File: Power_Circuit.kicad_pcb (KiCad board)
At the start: 2 copper layers, 168.9 x 77.5 mm, 45 parts, among them J1 Conn_01x09, J2 Conn_01x04, K1 DSP1A-L2-DC5V, Q1 IRF7606PBF_3PINS_BWOUF, SW1 SW_Push, SW2 SW_STARTER, U1 B_Plug_Battery_In, U10 DSN2596, U11 B_Plug_12v_Motor1, U12 B_Plug_12v_Motor2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

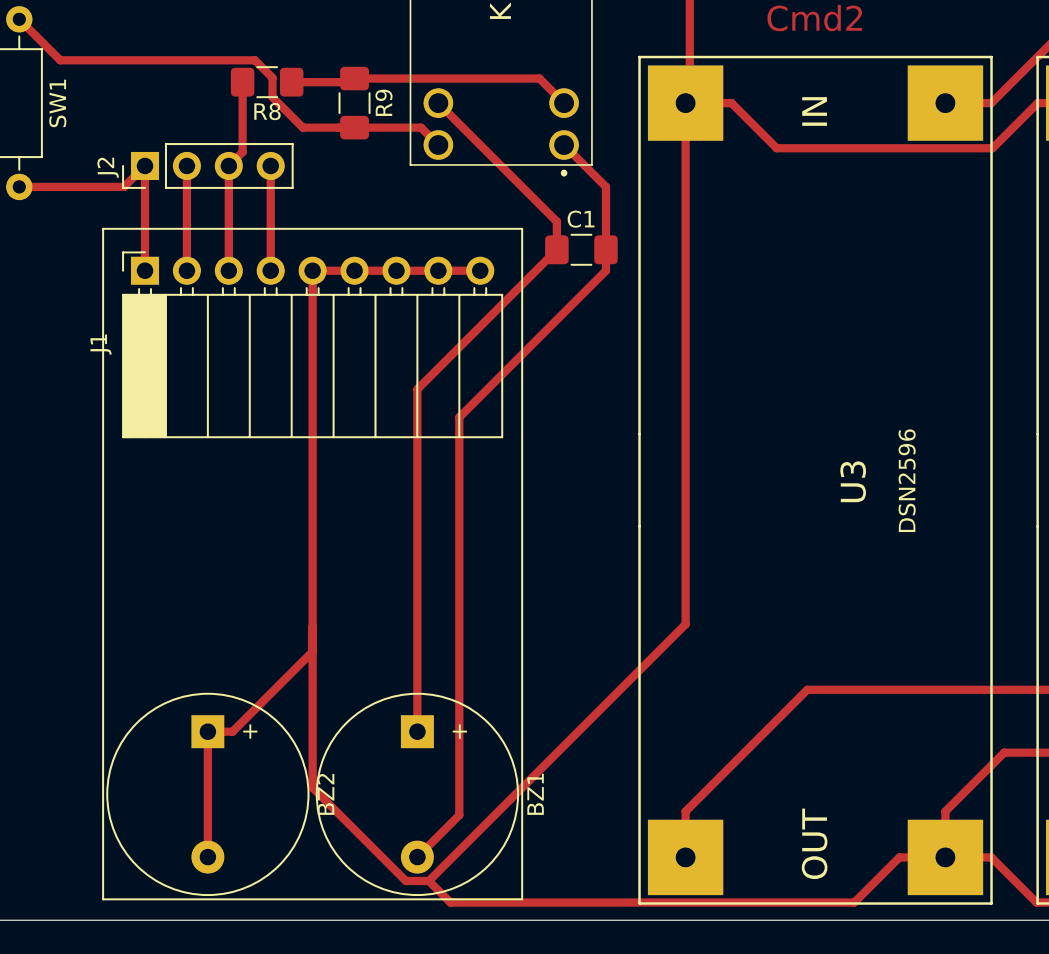
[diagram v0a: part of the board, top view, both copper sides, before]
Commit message: Changement pour ajouter la possibiliter de court circuiter les 2 buzzers ou 1
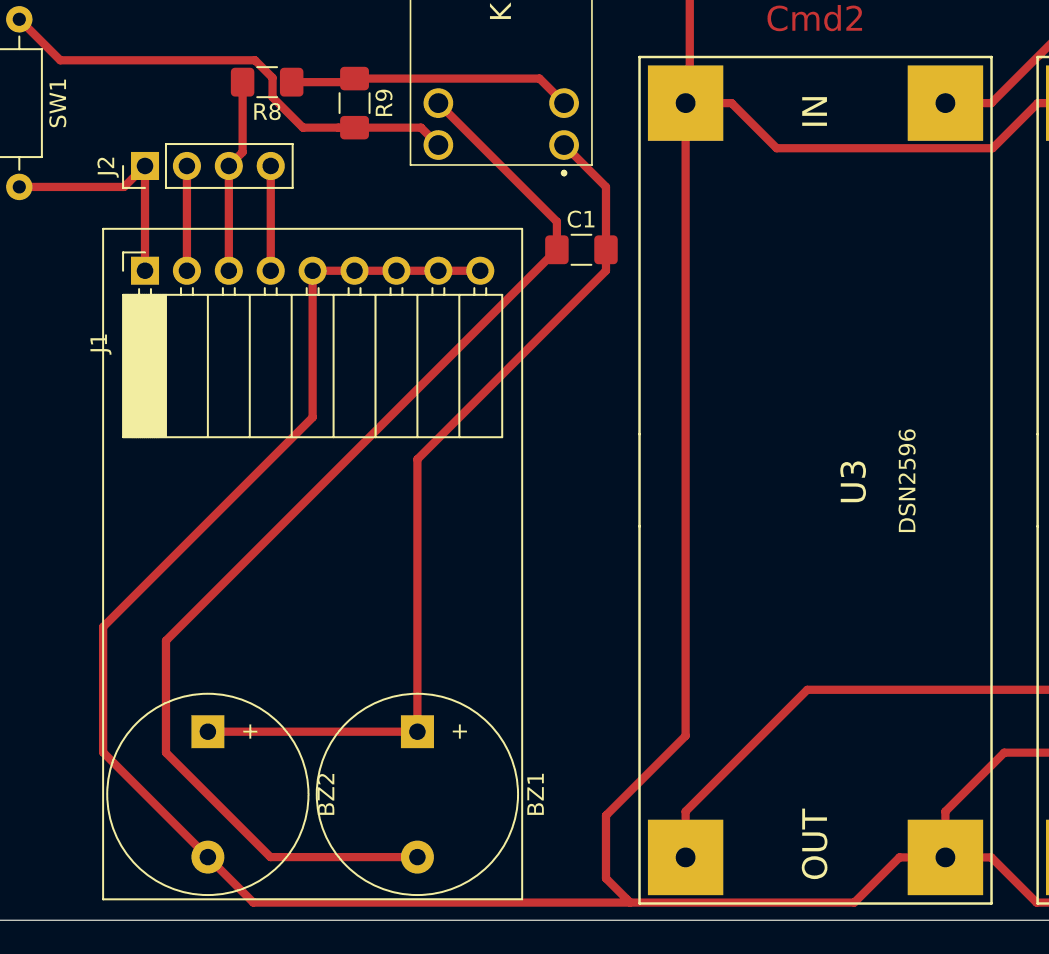
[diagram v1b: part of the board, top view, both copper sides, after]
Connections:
- BZ1 pad 1: /PowerProtection/Buzzer+ -> /PowerProtection/Buzzer-
- BZ1 pad 2: /PowerProtection/Buzzer- -> /PowerProtection/Buzzer+
- BZ2 pad 1: GND -> /PowerProtection/Buzzer-
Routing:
- net /PowerProtection/Buzzer+: track 44.6 -> 70.0 mm
- net /PowerProtection/Buzzer-: track 48.9 -> 54.0 mm
- net GND: track 797.1 -> 793.8 mm
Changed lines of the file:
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@@
     (thickness 1.6)
     (drawings 22)
-    (tracks 245)
+    (tracks 246)
     (zones 0)
     (modules 45)
@@
       (net 3 GND))
     (pad 1 thru_hole rect (at 0 0 270) (size 2 2) (drill 1) (layers *.Cu *.Mask)
-      (net 3 GND))
+      (net 2 /PowerProtection/Buzzer-))
     (model ${KISYS3DMOD}/Buzzer_Beeper.3dshapes/Buzzer_12x9.5RM7.6.wrl
       (at (xyz 0 0 0))
@@
     (fp_circle (center 3.8 0) (end 9.9 0) (layer F.SilkS) (width 0.12))
     (pad 1 thru_hole rect (at 0 0 270) (size 2 2) (drill 1) (layers *.Cu *.Mask)
+      (net 2 /PowerProtection/Buzzer-))
+    (pad 2 thru_hole circle (at 7.6 0 270) (size 2 2) (drill 1) (layers *.Cu *.Mask)
       (net 1 /PowerProtection/Buzzer+))
-    (pad 2 thru_hole circle (at 7.6 0 270) (size 2 2) (drill 1) (layers *.Cu *.Mask)
-      (net 2 /PowerProtection/Buzzer-))
     (model ${KISYS3DMOD}/Buzzer_Beeper.3dshapes/Buzzer_12x9.5RM7.6.wrl
       (at (xyz 0 0 0))
@@
   (segment (start 95.25 95.25) (end 102.435 102.435) (width 0.5) (layer F.Cu) (net 1))
   (segment (start 102.435 102.435) (end 102.435 104.14) (width 0.5) (layer F.Cu) (net 1))
-  (segment (start 93.98 112.595) (end 102.435 104.14) (width 0.5) (layer F.Cu) (net 1))
-  (segment (start 93.98 133.35) (end 93.98 112.595) (width 0.5) (layer F.Cu) (net 1))
-  (segment (start 93.98 140.95) (end 96.52 138.41) (width 0.5) (layer F.Cu) (net 2))
-  (segment (start 96.52 138.41) (end 96.52 114.3) (width 0.5) (layer F.Cu) (net 2))
-  (segment (start 105.41 105.41) (end 105.41 104.14) (width 0.5) (layer F.Cu) (net 2))
-  (segment (start 96.52 114.3) (end 105.41 105.41) (width 0.5) (layer F.Cu) (net 2))
+  (segment (start 85.07 140.95) (end 93.98 140.95) (width 0.5) (layer F.Cu) (net 1))
+  (segment (start 78.74 134.62) (end 85.07 140.95) (width 0.5) (layer F.Cu) (net 1))
+  (segment (start 102.435 104.14) (end 78.74 127.835) (width 0.5) (layer F.Cu) (net 1))
+  (segment (start 78.74 127.835) (end 78.74 134.62) (width 0.5) (layer F.Cu) (net 1))
   (segment (start 105.41 100.33) (end 102.87 97.79) (width 0.5) (layer F.Cu) (net 2))
   (segment (start 105.41 104.14) (end 105.41 100.33) (width 0.5) (layer F.Cu) (net 2))
+  (segment (start 93.98 133.35) (end 81.28 133.35) (width 0.5) (layer F.Cu) (net 2))
+  (segment (start 93.98 116.84) (end 93.98 133.35) (width 0.5) (layer F.Cu) (net 2))
+  (segment (start 105.41 104.14) (end 105.41 105.41) (width 0.5) (layer F.Cu) (net 2))
+  (segment (start 105.41 105.41) (end 93.98 116.84) (width 0.5) (layer F.Cu) (net 2))
   (segment (start 87.63 105.41) (end 97.79 105.41) (width 0.5) (layer F.Cu) (net 3))
   (segment (start 114.3 81.4975) (end 110.49 85.3075) (width 0.5) (layer F.Cu) (net 3))
@@
   (segment (start 110.49 94.996) (end 110.236 95.25) (width 0.5) (layer F.Cu) (net 3))
   (segment (start 110.49 85.3075) (end 110.49 94.996) (width 0.5) (layer F.Cu) (net 3))
-  (segment (start 87.63 106.612081) (end 87.63 105.41) (width 0.5) (layer F.Cu) (net 3))
-  (segment (start 93.283999 142.400001) (end 87.63 136.746002) (width 0.5) (layer F.Cu) (net 3))
-  (segment (start 94.676001 142.400001) (end 93.283999 142.400001) (width 0.5) (layer F.Cu) (net 3))
-  (segment (start 110.236 126.840002) (end 94.676001 142.400001) (width 0.5) (layer F.Cu) (net 3))
-  (segment (start 110.236 95.25) (end 110.236 126.840002) (width 0.5) (layer F.Cu) (net 3))
   (segment (start 113.022 95.25) (end 110.236 95.25) (width 0.5) (layer F.Cu) (net 3))
   (segment (start 115.758001 97.986001) (end 113.022 95.25) (width 0.5) (layer F.Cu) (net 3))
@@
   (segment (start 230.85001 106.96999) (end 230.85001 103.15999) (width 0.5) (layer F.Cu) (net 3))
   (segment (start 230.85001 103.15999) (end 230.85001 99.34999) (width 0.5) (layer F.Cu) (net 3))
-  (segment (start 95.982001 143.706001) (end 94.676001 142.400001) (width 0.5) (layer F.Cu) (net 3))
-  (segment (start 120.461999 143.706001) (end 95.982001 143.706001) (width 0.5) (layer F.Cu) (net 3))
-  (segment (start 123.198 140.97) (end 120.461999 143.706001) (width 0.5) (layer F.Cu) (net 3))
-  (segment (start 125.984 140.97) (end 123.198 140.97) (width 0.5) (layer F.Cu) (net 3))
   (segment (start 205.994 125.476) (end 204.47 125.476) (width 0.5) (layer F.Cu) (net 3))
   (segment (start 212.09 119.38) (end 205.994 125.476) (width 0.5) (layer F.Cu) (net 3))
@@
   (segment (start 151.13 124.46) (end 151.13 100.33) (width 0.5) (layer F.Cu) (net 3))
   (segment (start 151.13 100.33) (end 152.4 99.06) (width 0.5) (layer F.Cu) (net 3))
-  (segment (start 81.28 133.35) (end 81.28 140.95) (width 0.5) (layer F.Cu) (net 3))
-  (segment (start 82.78 133.35) (end 87.63 128.5) (width 0.5) (layer F.Cu) (net 3))
-  (segment (start 81.28 133.35) (end 82.78 133.35) (width 0.5) (layer F.Cu) (net 3))
-  (segment (start 87.63 128.5) (end 87.63 127) (width 0.5) (layer F.Cu) (net 3))
-  (segment (start 87.63 136.746002) (end 87.63 127) (width 0.5) (layer F.Cu) (net 3))
-  (segment (start 87.63 127) (end 87.63 106.612081) (width 0.5) (layer F.Cu) (net 3))
+  (segment (start 87.63 105.41) (end 87.63 114.3) (width 0.5) (layer F.Cu) (net 3))
+  (segment (start 87.63 114.3) (end 74.93 127) (width 0.5) (layer F.Cu) (net 3))
+  (segment (start 74.93 134.6) (end 81.28 140.95) (width 0.5) (layer F.Cu) (net 3))
+  (segment (start 74.93 127) (end 74.93 134.6) (width 0.5) (layer F.Cu) (net 3))
+  (segment (start 123.198 140.97) (end 125.984 140.97) (width 0.5) (layer F.Cu) (net 3))
+  (segment (start 120.461999 143.706001) (end 123.198 140.97) (width 0.5) (layer F.Cu) (net 3))
+  (segment (start 81.28 140.95) (end 84.036001 143.706001) (width 0.5) (layer F.Cu) (net 3))
+  (segment (start 110.236 95.25) (end 110.236 133.604) (width 0.5) (layer F.Cu) (net 3))
+  (segment (start 110.236 133.604) (end 105.41 138.43) (width 0.5) (layer F.Cu) (net 3))
+  (segment (start 105.41 138.43) (end 105.41 142.24) (width 0.5) (layer F.Cu) (net 3))
+  (segment (start 105.41 142.24) (end 106.68 143.51) (width 0.5) (layer F.Cu) (net 3))
+  (segment (start 106.68 143.51) (end 106.876001 143.706001) (width 0.5) (layer F.Cu) (net 3))
+  (segment (start 84.036001 143.706001) (end 106.876001 143.706001) (width 0.5) (layer F.Cu) (net 3))
+  (segment (start 106.876001 143.706001) (end 120.461999 143.706001) (width 0.5) (layer F.Cu) (net 3))
   (segment (start 114.0714 75.9825) (end 114.3 76.2111) (width 0.5) (layer F.Cu) (net 4))
   (segment (start 110.49 75.9825) (end 114.0714 75.9825) (width 0.5) (layer F.Cu) (net 4))

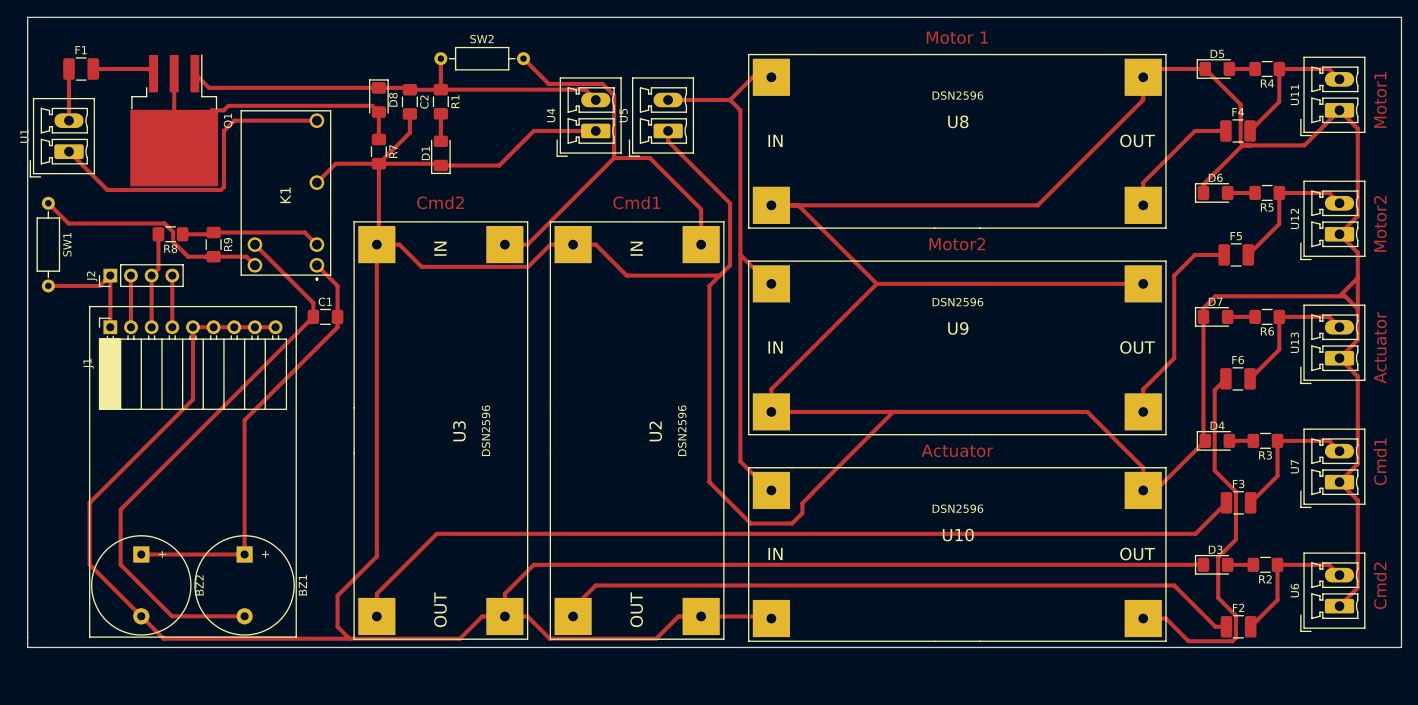
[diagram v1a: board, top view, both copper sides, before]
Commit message: Avec regul moteur et texte sur autre couche
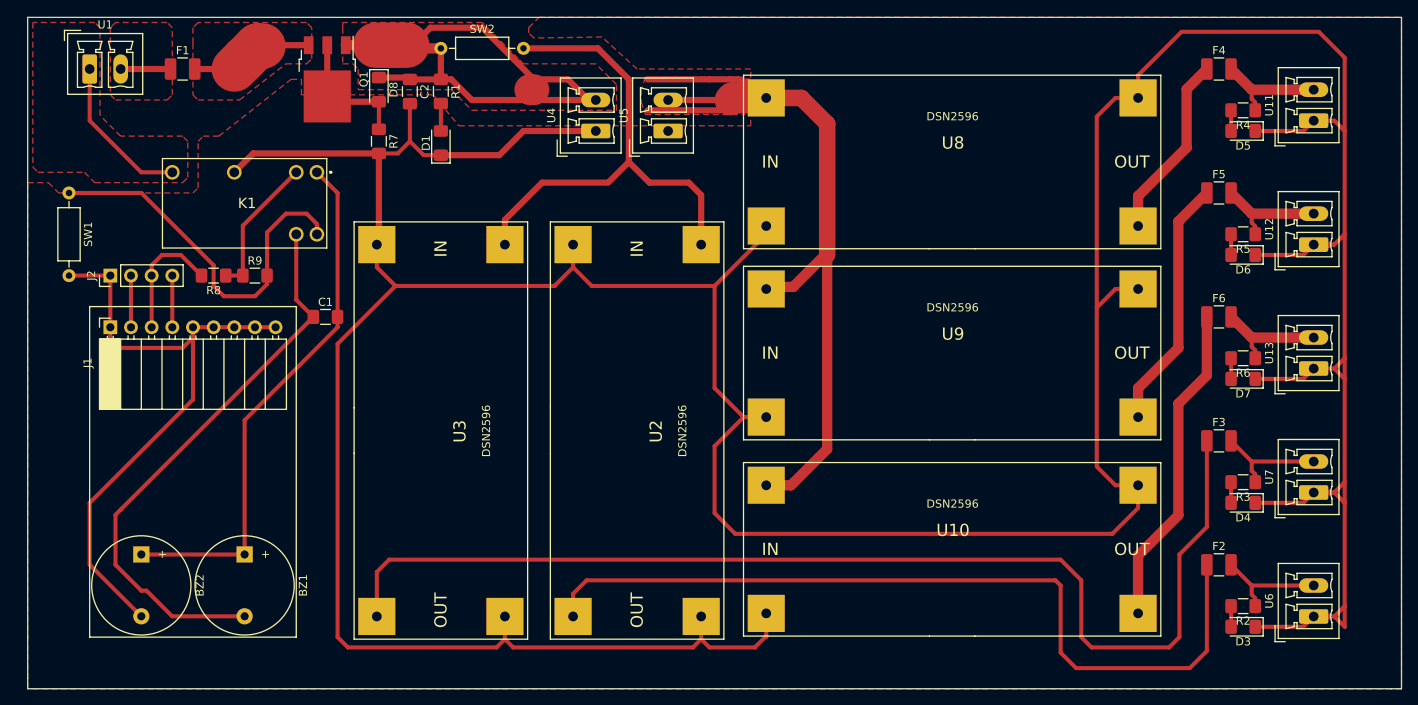
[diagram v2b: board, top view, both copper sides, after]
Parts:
- Q1: footprint Package_TO_SOT_SMD:TO-263-3_TabPin2 -> Package_TO_SOT_SMD:TO-252-3_TabPin2
- U11: value B_Plug_12v_Motor1 -> B_Plug_18v_Motor1
- U12: value B_Plug_12v_Motor2 -> B_Plug_18v_Motor2
- moved Q1 19.5 mm to (104.1, 74.9)
- moved F1 12.5 mm to (86.4, 73.7)
- moved K1 11.4 mm to (102.9, 86.4), turned to 180 degrees
- moved U1 10.5 mm to (74.9, 73.7), turned to 0 degrees
- moved D3 8.34 mm to (216.8, 142.2), turned to 180 degrees
- moved D7 8.34 mm to (216.8, 111.8), turned to 180 degrees
- moved D6 8.34 mm to (216.8, 96.5), turned to 180 degrees
- moved D4 8.26 mm to (216.8, 127.0), turned to 180 degrees
- moved D5 8.26 mm to (216.8, 81.3), turned to 180 degrees
- moved F2 7.99 mm to (213.8, 134.6)
- moved F3 7.99 mm to (213.8, 119.4)
- moved F4 7.97 mm to (213.8, 73.7)
- moved F6 7.97 mm to (213.8, 104.1)
- moved F5 7.91 mm to (213.8, 88.9)
- moved R8 7.34 mm to (90.2, 99.1)
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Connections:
- net 12V_Motor1 renamed 18V_Motor1
- net 12V_Motor2 renamed 18V_Motor2
- BZ2 pad 2: GND -> Net-(BZ2-Pad2)
- J1 pad 1: Net-(J1-Pad1) -> Net-(BZ2-Pad2)
- J1 pad 5: GND -> Net-(BZ2-Pad2)
- J1 pad 6: GND -> Net-(BZ2-Pad2)
- J1 pad 7: GND -> Net-(BZ2-Pad2)
- J1 pad 8: GND -> Net-(BZ2-Pad2)
- J1 pad 9: GND -> Net-(BZ2-Pad2)
- J2 pad 1: Net-(J1-Pad1) -> Net-(BZ2-Pad2)
- SW1 pad 2: Net-(J1-Pad1) -> Net-(BZ2-Pad2)
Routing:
- net GND: track 793.8 -> 562.1 mm
- net Net-(BZ2-Pad2): track 0.00 -> 78.8 mm
- net 18V: track 69.4 -> 102.8 mm
- net Net-(F3-Pad1): track 111.9 -> 139.4 mm
- net Net-(D8-Pad2): track 40.2 -> 16.3 mm
- net /PowerProtection/BatteryPowerIn-: track 40.0 -> 19.1 mm
- net 18V_Battery: track 54.5 -> 73.9 mm
- net /PowerProtection/BalanceGND: track 29.2 -> 47.0 mm
- net Net-(F2-Pad1): track 84.6 -> 102.2 mm
- net Net-(J1-Pad1): track 14.5 -> 0.00 mm
- net /PowerProtection/Buzzer-: track 54.0 -> 65.5 mm
- net Net-(F6-Pad1): track 48.0 -> 40.0 mm
- net Net-(F1-Pad2): track 7.66 -> 15.2 mm
- net Net-(F4-Pad1): track 15.6 -> 22.8 mm
- net Net-(SW2-Pad2): track 56.2 -> 62.3 mm
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- added copper zone on F.Cu, net /PowerProtection/BatteryPowerIn+
- added copper zone on F.Cu, net /PowerProtection/BatteryPowerIn-
- added copper zone on F.Cu, net 18V
- added copper zone on F.Cu, net 18V_Battery
- added copper zone on F.Cu, net GND
- added copper zone on F.Cu, net Net-(F1-Pad2)
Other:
- board size 168.9 x 77.5 mm -> 168.9 x 82.6 mm
- board text added: "Actuator-5V"
- board text added: "Cmd-5V"
- board text added: "Cmd-7V5"
- board text added: "Cmd-7v5"
- board text added: "Don't solder those buzzers"
- board text added: "Motor1-18V"
- board text added: "Motor2-18V"
- board text removed: "Actuator"
- board text removed: "Cmd1"
- board text removed: "Cmd2"
- board text removed: "Don't solder this buzzer"
- board text removed: "Motor 1"
- board text removed: "Motor1"
- board text removed: "Motor2"

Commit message: Ajout BOM, suppression tirette, correction silk, correction des plans pour meilleur refroidissement du transistor notamment
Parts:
- removed SW2: SW_STARTER, LIB_BE_PHELMA:R_Axial_DIN0207_L6.3mm_D2.5mm_P10.16mm_Horizontal
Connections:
- U2 pad 1: Net-(SW2-Pad2) -> 18V_Battery
- U3 pad 1: Net-(SW2-Pad2) -> 18V_Battery
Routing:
- net Net-(SW2-Pad2): track 62.3 -> 0.00 mm
- net 18V_Battery: track 73.9 -> 128.2 mm
- net 18V: track 102.8 -> 93.5 mm
- added copper zone on F.Cu, net Net-(D8-Pad2)
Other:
- board text added: "Motor1-12V"
- board text added: "Motor2-12V"
- board text removed: "Motor1-18V"
- board text removed: "Motor2-18V"
